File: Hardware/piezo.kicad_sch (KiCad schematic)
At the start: 0 parts

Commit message: Piezo transducer driver added(transistor amplifier part).
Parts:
- added C? (x5): C_Small, symbol Device:C_Small
- added C? (x2): 100n, symbol Device:C_Small
- added C? (x2): 12p %5, Capacitor_SMD:C_0603_1608Metric_Pad1.08x0.95mm_HandSolder, symbol Device:C_Small
- added C?: 100n, Capacitor_SMD:C_0603_1608Metric_Pad1.08x0.95mm_HandSolder, symbol Device:C_Small
- added C?: 220u, symbol LibreSolar:CP
- added C?: 10u, symbol Device:C_Small
- added D? (x2): 1N4148, symbol Device:D_Small
- added J?: AudioJack2, symbol Connector:AudioJack2
- added Q? (x2): BCP53-16, Package_TO_SOT_SMD:SOT-223-3_TabPin2, symbol Transistor_BJT:BCP53
- added Q? (x2): BC817, Package_TO_SOT_SMD:SOT-23, symbol Transistor_BJT:BC817
- added Q?: MJD44H11T4G, symbol Device:Q_PNP_BCE
- added Q?: MJD45H11T4G, symbol Device:Q_NPN_BCE
- added Q? (x2): BCP56-16, Package_TO_SOT_SMD:SOT-223-3_TabPin2, symbol Transistor_BJT:BCP56
- added R? (x9): R_Small, symbol Device:R_Small
- added R?: 8.2k %1, Resistor_SMD:R_0603_1608Metric_Pad0.98x0.95mm_HandSolder, symbol Device:R_Small
- added R? (x4): 33R %1, Resistor_SMD:R_0603_1608Metric_Pad0.98x0.95mm_HandSolder, symbol Device:R_Small
- added R? (x3): 2.2k %1, Resistor_SMD:R_0603_1608Metric_Pad0.98x0.95mm_HandSolder, symbol Device:R_Small
- added R? (x2): 422R %1, Resistor_SMD:R_0603_1608Metric_Pad0.98x0.95mm_HandSolder, symbol Device:R_Small
- added R? (x2): 0.33R, Resistor_SMD:R_2512_6332Metric_Pad1.40x3.35mm_HandSolder, symbol Device:R_Small
- added R?: 1.2k %1, Resistor_SMD:R_0603_1608Metric_Pad0.98x0.95mm_HandSolder, symbol Device:R_Small
- added U? (x2): Opamp_Dual, symbol Device:Opamp_Dual
- added U? (x3): LM7322, symbol Device:Opamp_Dual
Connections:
- new net: C?.1, R?.1, R?.2 (x2)
- new net: C?.2, R?.1, U?.1, U?.2 (-) (x2)
- new net: Q?.1 (B), Q?.3 (C), R?.1 (x2)
- new net: C?.2, Q?.1 (B), Q?.1 (B), Q?.2 (C), Q?.2 (C), Q?.4 (C), Q?.4 (C)
- new net: Q?.3 (E), R?.1 (x3)
- new net: R?.1, U?.1
- new net: R?.1, R?.2, U?.2 (-)
- new net: R?.1, R?.2, U?.5 (+)
- new net: J?.T, R?.1, R?.1, R?.1, R?.2
- new net: C?.1, Q?.1 (B), R?.2, R?.2
- new net: C?.1, Q?.1 (B), R?.1, R?.2
- new net: Q?.2 (E), Q?.2 (E), R?.2
- new net: C?.1, D?.1 (K), Q?.1 (B), Q?.2 (C), Q?.4 (C)
- new net: Q?.3 (E), R?.2 (x3)
- new net: C?.1, R?.2, U?.3 (+) (x2)
- new net: C?.2, C?.2, D?.2 (A), Q?.1 (B), Q?.2 (C), Q?.4 (C)
- new net: C?.1, R?.2
- new net: C?.2, J?.S, R?.1
- new net: D?.1 (K), D?.2 (A)
- new net +24V: C?.1, C?.1, C?.1, C?.1, Q?.2 (C), R?.2, R?.2, R?.2, R?.2, R?.2
- new net +5VA: U?.8 (V+)
- new net GND: C?.2, C?.2, C?.2, C?.2, C?.2, C?.2, Q?.2 (C), R?.1, R?.1, R?.1, R?.1, R?.2, R?.2, U?.4 (V-)
- new net amplifier_in: R?.1

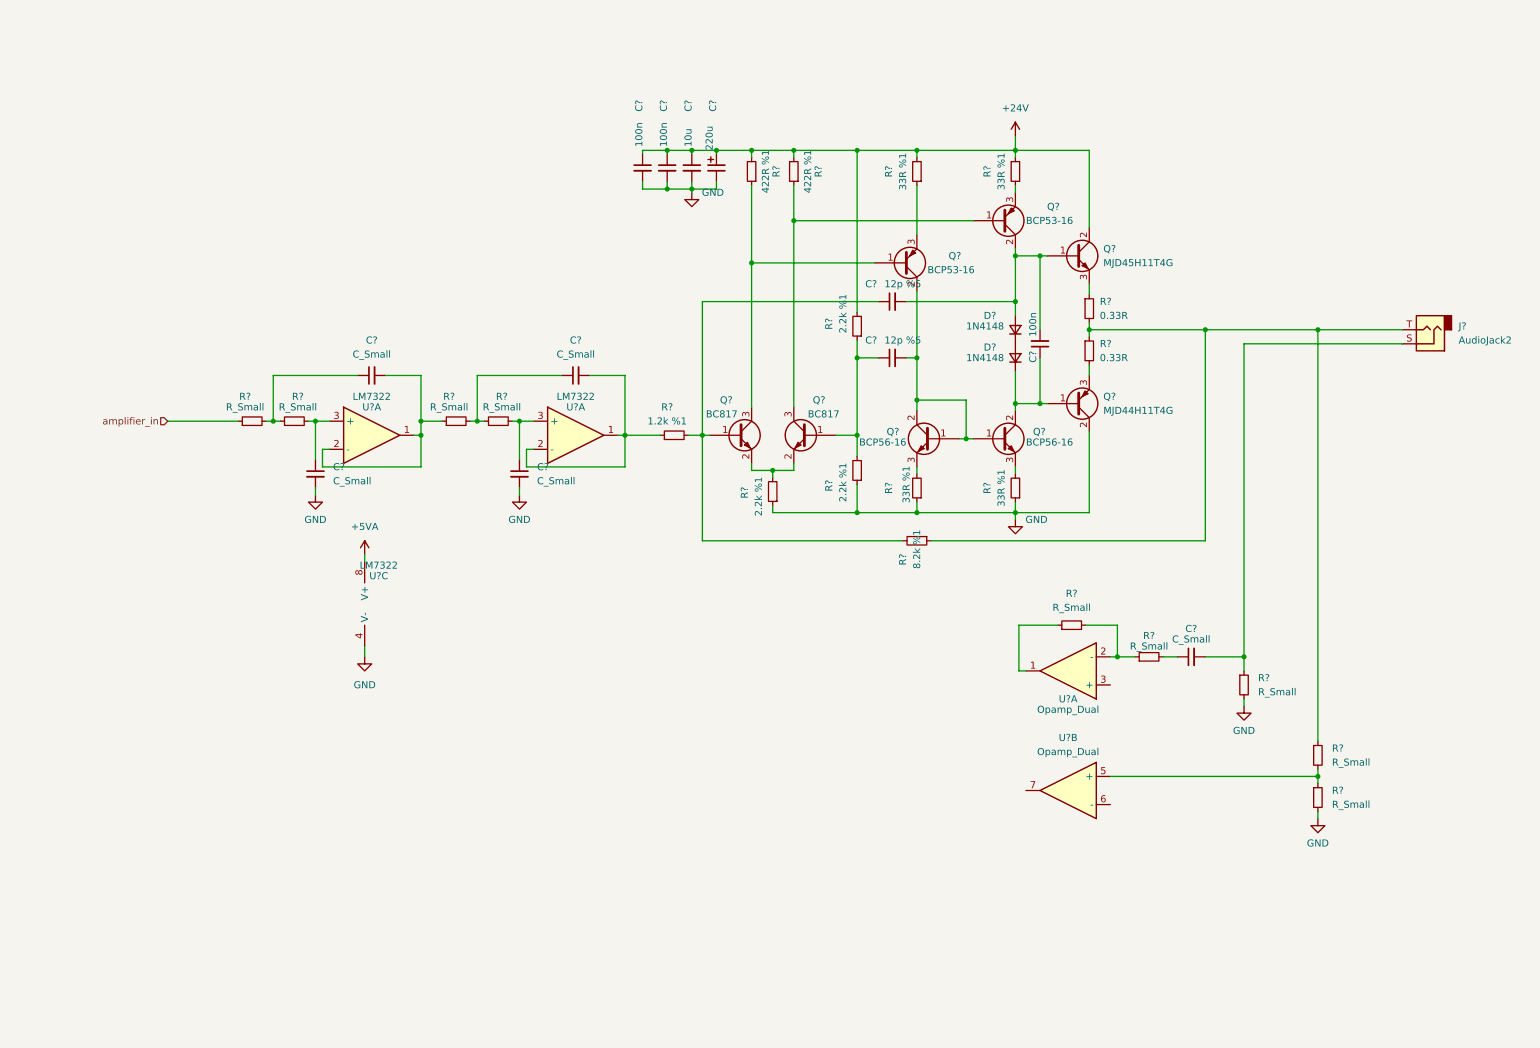
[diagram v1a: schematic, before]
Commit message: Changes about piezo transducer driver
+ Regarding measurement of piezo transducer impedance, driver circuit is updated.(-+15v). Besides circuit is updated. But yet to be simulated for new resistance values.
+ Most cost efficient analog design(up to now) is created. Noise free enough, but nothing more.
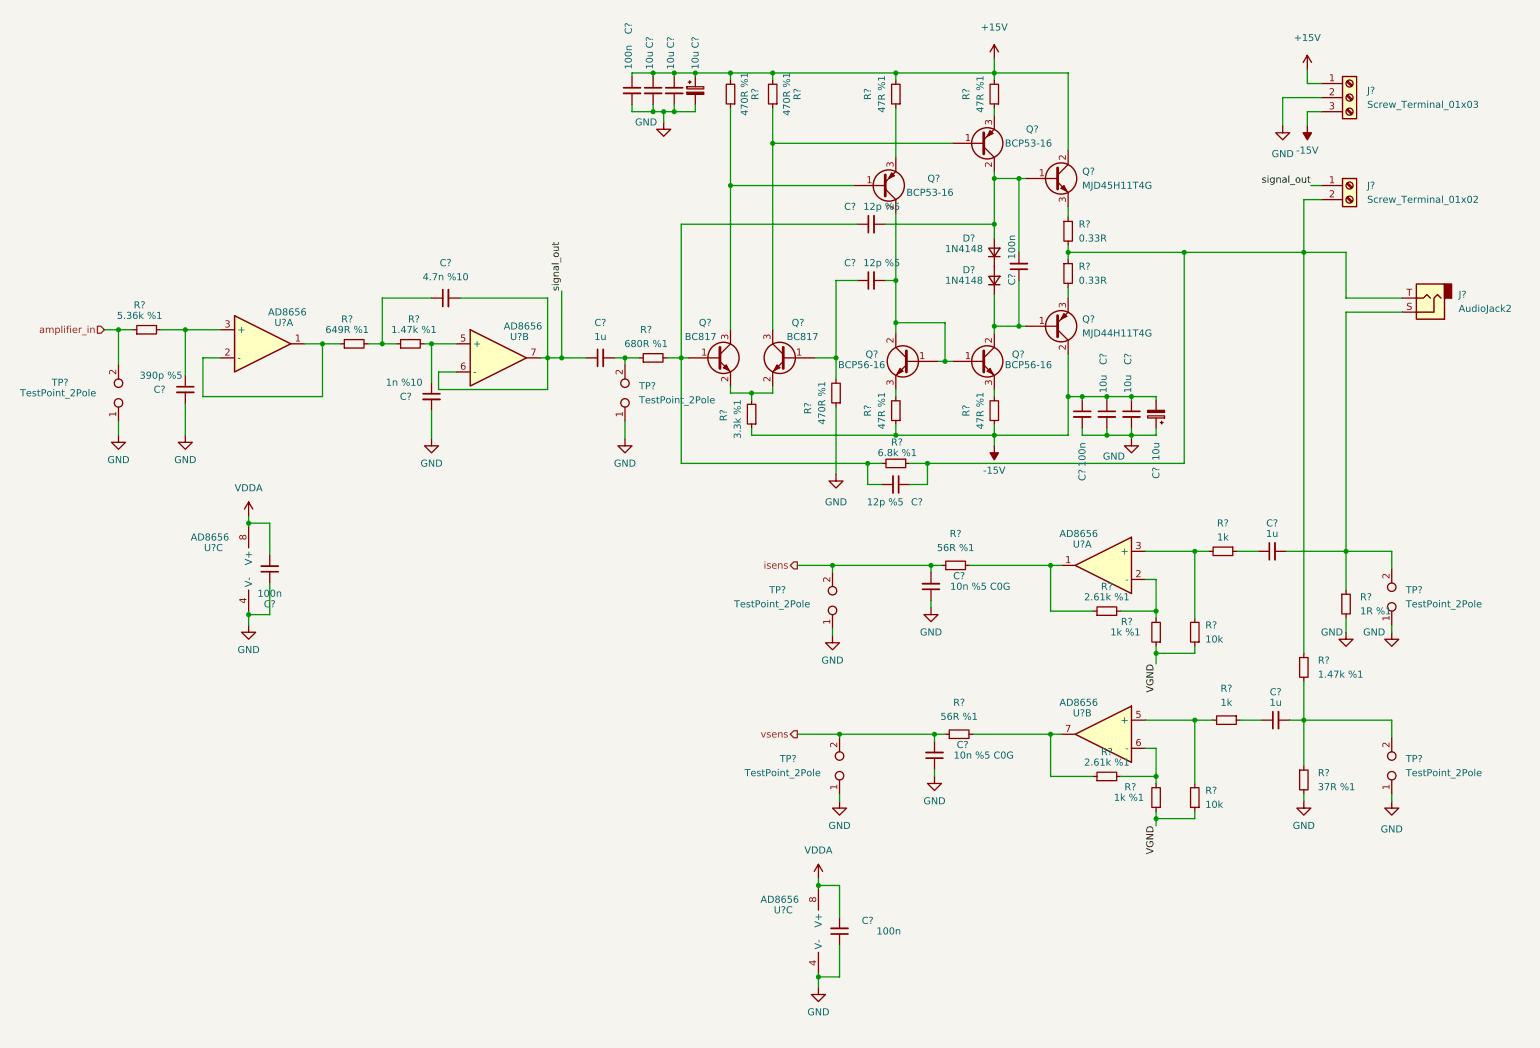
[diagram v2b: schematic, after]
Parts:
- removed C? (x3): C_Small, symbol Device:C_Small
- removed C?: 220u, symbol LibreSolar:CP
- removed C?: 10u, symbol Device:C_Small
- removed C?: 100n, symbol Device:C_Small
- removed R? (x6): R_Small, symbol Device:R_Small
- removed R? (x3): 33R %1, Resistor_SMD:R_0603_1608Metric_Pad0.98x0.95mm_HandSolder, symbol Device:R_Small
- removed R?: 422R %1, Resistor_SMD:R_0603_1608Metric_Pad0.98x0.95mm_HandSolder, symbol Device:R_Small
- removed R?: 2.2k %1, Resistor_SMD:R_0603_1608Metric_Pad0.98x0.95mm_HandSolder, symbol Device:R_Small
- removed U? (x2): Opamp_Dual, symbol Device:Opamp_Dual
- removed U? (x3): LM7322, symbol Device:Opamp_Dual
- added C? (x2): 10n %5 C0G, Capacitor_SMD:C_0603_1608Metric_Pad1.08x0.95mm_HandSolder, symbol Device:C_Small
- added C? (x2): 100n, Capacitor_SMD:C_0603_1608Metric_Pad1.08x0.95mm_HandSolder, symbol Device:C_Small
- added C?: 12p %5, Capacitor_SMD:C_0603_1608Metric_Pad1.08x0.95mm_HandSolder, symbol Device:C_Small
- added C? (x4): 10u, symbol Device:C_Small
- added C? (x2): 1u, symbol Device:C_Small
- added C?: 100n, symbol Device:C_Small
- added C?: 390p %5, symbol Device:C_Small
- added C?: 1n %10, symbol Device:C_Small
- added C? (x2): 10u, symbol Device:C_Polarized_Small
- added J?: Screw_Terminal_01x03, symbol Connector:Screw_Terminal_01x03
- added J?: Screw_Terminal_01x02, symbol Connector:Screw_Terminal_01x02
- added R? (x2): 1k %1, symbol Device:R_Small
- added R? (x3): 47R %1, Resistor_SMD:R_0603_1608Metric_Pad0.98x0.95mm_HandSolder, symbol Device:R_Small
- added R?: 5.36k %1, Resistor_SMD:R_0603_1608Metric_Pad0.98x0.95mm_HandSolder, symbol Device:R_Small
- added R?: 470R %1, Resistor_SMD:R_0603_1608Metric_Pad0.98x0.95mm_HandSolder, symbol Device:R_Small
- added R? (x2): 2.61k %1, symbol Device:R_Small
- added R? (x2): 1k, symbol Device:R_Small
- added R?: 37R %1, symbol Device:R_Small
- added R?: 1.47k %1, symbol Device:R_Small
- added R? (x2): 56R %1, symbol Device:R_Small
- added R? (x2): 10k, symbol Device:R_Small
- added TP? (x6): TestPoint_2Pole, symbol Connector:TestPoint_2Pole
- added U? (x6): AD8656, Package_SO:SOIC-8_3.9x4.9mm_P1.27mm, symbol Device:Opamp_Dual
- C?: value C_Small -> 4.7n %10
- C?: value C_Small -> 1u
- R?: value 8.2k %1 -> 6.8k %1; Link https://ozdisan.com/passive-components/resistors/smt-smd-an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 -> (none); Price 0.00221 -> (none)
- R?: value 2.2k %1 -> 470R %1; Link https://ozdisan.com/passive-components/resistors/smt-smd-an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 -> (none); Price 0.00221 -> (none)
- R?: value R_Small -> 649R %1; footprint (none) -> Resistor_SMD:R_0603_1608Metric_Pad0.98x0.95mm_HandSolder
- R?: value 2.2k %1 -> 3.3k %1; Link https://ozdisan.com/passive-components/resistors/smt-smd-an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 -> (none); Price 0.00221 -> (none)
- R?: value R_Small -> 1R %1
- R?: value R_Small -> 1.47k %1; footprint (none) -> Resistor_SMD:R_0603_1608Metric_Pad0.98x0.95mm_HandSolder
- R?: value 422R %1 -> 470R %1; Link https://ozdisan.com/passive-components/resistors/smt-smd-an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 -> (none); Price 0.00364 -> (none)
- R?: value 1.2k %1 -> 680R %1; Link https://ozdisan.com/passive-components/resistors/smt-smd-an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 -> (none); Price 0.00221 -> (none)
- R?: value 33R %1 -> 47R %1; Link https://ozdisan.com/passive-components/resistors/smt-smd-an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 -> (none); Price 0.00221 -> (none)
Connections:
- net GND: now also C?.1, C?.1, C?.1, C?.1, C?.1, C?.2, C?.2, C?.2, C?.2, C?.2, C?.2, C?.2, C?.2, J?.2 (Pin_2), R?.2, TP?.1, TP?.1, TP?.1, TP?.1, TP?.1, TP?.1, U?.4 (V-), U?.4 (V-); no longer Q?.2 (C), R?.1
- net amplifier_in: now also R?.1, TP?.2; no longer R?.1
- net signal_out: now reaches C?.2
- net signal_out: now also C?.1, J?.1 (Pin_1), U?.6 (-), U?.7
- net at J?.T, R?.1, R?.1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: now also C?.1, J?.2 (Pin_2), R?.1
- net at C?.1, Q?.1 (B), R?.2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: now also C?.2
- net at Q?.1 (B), Q?.3 (C): now also R?.1
- net at Q?.3 (E): now also R?.1
- net at R?.2: now also C?.1, U?.5 (+)
- net at C?.1: now also R?.1
- net at Q?.3 (E): now also R?.2 (x2)
- net at R?.1: now also C?.2, TP?.2
- net at C?.2, J?.S, R?.1: now also TP?.2
- net +24V renamed +15V
- net +15V: now also C?.1, C?.1, C?.1, J?.1 (Pin_1), R?.2, R?.2
- new net: R?.1, U?.1, U?.2 (-)
- new net: C?.1, R?.2, U?.3 (+)
- new net: R?.2, R?.2, U?.5 (+)
- new net: R?.2, R?.2, U?.6 (-)
- new net: R?.1, R?.2, U?.7
- new net: R?.2, R?.2, U?.2 (-)
- new net: R?.1, R?.2, U?.1
- new net: R?.2, R?.2, U?.3 (+)
- new net: C?.2, R?.1, R?.2, TP?.2
- new net: C?.1, R?.1
- new net -15V: C?.1, C?.1, C?.1, C?.2, J?.3 (Pin_3), Q?.2 (C), R?.1, R?.1, R?.1
- new net VDDA: C?.2, C?.2, U?.8 (V+), U?.8 (V+)
- new net VGND: R?.1, R?.1, R?.1, R?.1
- new net isens: C?.2, R?.1, TP?.2
- new net vsens: C?.2, R?.1, TP?.2
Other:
- moved on the sheet: C?, D?, J?, Q?, R?

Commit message: Completed schematic and PCB.
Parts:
- removed C?: 4.7n %10, symbol Device:C_Small
- removed C? (x2): 12p %5, Capacitor_SMD:C_0603_1608Metric_Pad1.08x0.95mm_HandSolder, symbol Device:C_Small
- removed C?: 10n %5 C0G, Capacitor_SMD:C_0603_1608Metric_Pad1.08x0.95mm_HandSolder, symbol Device:C_Small
- removed C? (x4): 10u, symbol Device:C_Small
- removed C? (x3): 1u, symbol Device:C_Small
- removed C?: 390p %5, symbol Device:C_Small
- removed C?: 1n %10, symbol Device:C_Small
- removed C? (x2): 10u, symbol Device:C_Polarized_Small
- removed D?: 1N4148, symbol Device:D_Small
- removed J?: Screw_Terminal_01x03, symbol Connector:Screw_Terminal_01x03
- removed J?: Screw_Terminal_01x02, symbol Connector:Screw_Terminal_01x02
- removed Q? (x2): BCP53-16, Package_TO_SOT_SMD:SOT-223-3_TabPin2, symbol Transistor_BJT:BCP53
- removed Q? (x2): BC817, Package_TO_SOT_SMD:SOT-23, symbol Transistor_BJT:BC817
- removed R? (x2): 1k %1, symbol Device:R_Small
- removed R?: 5.36k %1, Resistor_SMD:R_0603_1608Metric_Pad0.98x0.95mm_HandSolder, symbol Device:R_Small
- removed R? (x2): 470R %1, Resistor_SMD:R_0603_1608Metric_Pad0.98x0.95mm_HandSolder, symbol Device:R_Small
- removed R? (x2): 2.61k %1, symbol Device:R_Small
- removed R? (x3): 47R %1, Resistor_SMD:R_0603_1608Metric_Pad0.98x0.95mm_HandSolder, symbol Device:R_Small
- removed R? (x2): 1k, symbol Device:R_Small
- removed R? (x2): 10k, symbol Device:R_Small
- removed R?: 1.47k %1, Resistor_SMD:R_0603_1608Metric_Pad0.98x0.95mm_HandSolder, symbol Device:R_Small
- removed R?: 680R %1, Resistor_SMD:R_0603_1608Metric_Pad0.98x0.95mm_HandSolder, symbol Device:R_Small
- removed R?: 56R %1, symbol Device:R_Small
- removed TP? (x5): TestPoint_2Pole, symbol Connector:TestPoint_2Pole
- removed U?: AD8656, Package_SO:SOIC-8_3.9x4.9mm_P1.27mm, symbol Device:Opamp_Dual
- added C? (x2): 6.8n %5, Capacitor_SMD:C_0805_2012Metric_Pad1.18x1.45mm_HandSolder, symbol Device:C_Small
- added C? (x3): 1u 25v, Capacitor_SMD:C_0603_1608Metric_Pad1.08x0.95mm_HandSolder, symbol Device:C_Small
- added C? (x4): 12p %5, Capacitor_SMD:C_0603_1608Metric_Pad1.08x0.95mm_HandSolder, symbol Device:C_Small
- added C? (x2): 10u 25V, Capacitor_SMD:C_1206_3216Metric_Pad1.33x1.80mm_HandSolder, symbol Device:C_Small
- added C?: 10n %5 C0G, Capacitor_SMD:C_0603_1608Metric_Pad1.08x0.95mm_HandSolder, symbol Device:C_Small
- added C?: 680p %5, Capacitor_SMD:C_0603_1608Metric_Pad1.08x0.95mm_HandSolder, symbol Device:C_Small
- added D?: 1N4148, Diode_SMD:D_SOD-123, symbol Device:D_Small
- added Q? (x2): BC817-40, Package_TO_SOT_SMD:SOT-23, symbol Transistor_BJT:BC817
- added Q? (x2): BCP53-16, Package_TO_SOT_SMD:SOT-223-3_TabPin2, symbol Transistor_BJT:BCP53
- added R? (x2): 536R %1, Resistor_SMD:R_0603_1608Metric_Pad0.98x0.95mm_HandSolder, symbol Device:R_Small
- added R?: 470R %1, Resistor_SMD:R_0603_1608Metric_Pad0.98x0.95mm_HandSolder, symbol Device:R_Small
- added R? (x4): 0R, symbol Device:R_Small
- added R? (x2): 1M, symbol Device:R_Small
- added R? (x2): 680R %1, Resistor_SMD:R_0603_1608Metric_Pad0.98x0.95mm_HandSolder, symbol Device:R_Small
- added R? (x2): 8.2k %1, Resistor_SMD:R_0603_1608Metric_Pad0.98x0.95mm_HandSolder, symbol Device:R_Small
- added R? (x3): 47R %1, Resistor_SMD:R_0603_1608Metric_Pad0.98x0.95mm_HandSolder, symbol Device:R_Small
- added R?: 2.2k %1, Resistor_SMD:R_0603_1608Metric_Pad0.98x0.95mm_HandSolder, symbol Device:R_Small
- added R?: 1430R %1, Resistor_SMD:R_0603_1608Metric_Pad0.98x0.95mm_HandSolder, symbol Device:R_Small
- added R?: 2.15k %1, Resistor_SMD:R_0603_1608Metric_Pad0.98x0.95mm_HandSolder, symbol Device:R_Small
- added R?: 56R %1, Resistor_SMD:R_0603_1608Metric_Pad0.98x0.95mm_HandSolder, symbol Device:R_Small
- added TP? (x6): TestPoint_2Pole, Connector_PinHeader_2.54mm:PinHeader_1x02_P2.54mm_Vertical, symbol Connector:TestPoint_2Pole
- added U?: AD8656, Package_SO:SOIC-8_3.9x4.9mm_P1.27mm, symbol Device:Opamp_Dual
- C? (x2): footprint (none) -> Capacitor_SMD:C_0603_1608Metric_Pad1.08x0.95mm_HandSolder; Link (none) -> https://ozdisan.com/passive-components/capacitors/smt-smd-a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
- C? (x2): Link (none) -> https://ozdisan.com/passive-components/capacitors/smt-smd-a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; Price (none) -> 0.00448
- D?: footprint (none) -> Diode_SMD:D_SOD-123; Link (none) -> https://ozdisan.com/power-semiconductors/diodes-diode-modul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; Price (none) -> 0.02794
- Q?: footprint (none) -> Package_TO_SOT_SMD:TO-252-2; Link (none) -> https://ozdisan.com/Product/Detail/448869/MJD44H11T4G; Price (none) -> 0.39273
- Q?: footprint (none) -> Package_TO_SOT_SMD:TO-252-2; Link (none) -> https://ozdisan.com/Product/Detail/448870/MJD45H11T4G; Price (none) -> 0.55649
- R?: value 6.8k %1 -> 8.2k %1; Link (none) -> https://ozdisan.com/passive-components/resistors/smt-smd-an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; Price (none) -> 0.00221
- R? (x3): Link (none) -> https://ozdisan.com/passive-components/resistors/smt-smd-an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; Price (none) -> 0.00221
- R?: value 649R %1 -> 887R %1; Link (none) -> https://ozdisan.com/passive-components/resistors/smt-smd-an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; Price (none) -> 0.00221
- R?: value 37R %1 -> 61.9R %1; footprint (none) -> Resistor_SMD:R_0603_1608Metric_Pad0.98x0.95mm_HandSolder; Link (none) -> https://ozdisan.com/passive-components/resistors/smt-smd-an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; Price (none) -> 0.00221
- R?: value 1.47k %1 -> 2.2k %1; footprint (none) -> Resistor_SMD:R_0603_1608Metric_Pad0.98x0.95mm_HandSolder; Link (none) -> https://ozdisan.com/passive-components/resistors/smt-smd-an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; Price (none) -> 0.00221
- R?: footprint (none) -> Resistor_SMD:R_0603_1608Metric_Pad0.98x0.95mm_HandSolder; Link (none) -> https://ozdisan.com/passive-components/resistors/smt-smd-an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; Price (none) -> 0.00221
- R?: value 1R %1 -> 1R 1/3W %1; footprint (none) -> Resistor_SMD:R_1210_3225Metric_Pad1.30x2.65mm_HandSolder; Link (none) -> https://ozdisan.com/passive-components/resistors/smt-smd-an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; Price (none) -> 0.05112
- TP?: footprint (none) -> Connector_PinHeader_2.54mm:PinHeader_1x02_P2.54mm_Vertical; Link (none) -> https://ozdisan.com/connectors-and-interconnects/headers/pi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; Price (none) -> 0.0091
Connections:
- net amplifier_in is gone; now on net SIGNAL: TP?.2
- net +15V: now also C?.1, R?.2, R?.2, R?.2
- net -15V: now also C?.1, R?.1
- net GND: now also C?.1, C?.2, C?.2, C?.2, C?.2, R?.1, TP?.1, TP?.1, TP?.1, TP?.1, TP?.1
- net at R?.2: now also C?.1, R?.1, R?.1
- net at R?.1: now also Q?.1 (B), Q?.3 (C)
- net at Q?.1 (B), Q?.1 (B), Q?.2 (C)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: now also C?.2, Q?.2 (C), Q?.4 (C), R?.1
- net at J?.S, R?.1: now also C?.2, TP?.2
- net at U?.1, U?.2 (-): now also R?.1; no longer R?.1
- net SIGNAL: now reaches U?.3 (+)
- net at J?.T, R?.1, R?.1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: now also C?.1, TP?.1
- net at R?.2: now also C?.2, R?.1; no longer C?.1
- net at R?.2: now also Q?.2 (E), Q?.2 (E)
- net at C?.1, Q?.1 (B), Q?.2 (C)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: now also D?.1 (K), R?.2
- net at R?.2: now also C?.1, R?.1, U?.7
- net at U?.2 (-): now also C?.2, R?.1, R?.1
- net at C?.2, C?.2, D?.2 (A)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: now also Q?.2 (C), Q?.4 (C), R?.2
- net at Q?.3 (E), R?.1: now also TP?.2
- net at U?.1: now also C?.1, R?.2, R?.2
- net v1.65: now reaches U?.3 (+)
- net v1.65: now also U?.5 (+), U?.5 (+)
- net at Q?.3 (E): now also R?.2
- net at R?.1, R?.2: now also C?.2, TP?.2
- net at D?.1 (K): now also D?.2 (A), R?.1
- net isens renamed ISENS
- net ISENS: now also R?.1, TP?.2
- net signal_out: no longer names the net of U?.6 (-)
- net signal_out: now also C?.1, R?.2; no longer U?.7
- net vsens renamed VSENS
- net VSENS: now also C?.2, TP?.2
- new net: Q?.1 (B), R?.1, R?.2, R?.2
- new net: Q?.1 (B), Q?.3 (C), R?.1
- new net: Q?.3 (E), R?.1 (x2)
- new net: C?.1, R?.2, R?.2
- new net: C?.1, R?.2 (x2)
- new net: C?.2, R?.2
- new net: C?.1, R?.1, R?.2
- new net: Q?.1 (B), R?.1, R?.2
- new net: C?.2, R?.1, R?.2, U?.6 (-)
- new net: C?.1, R?.1, R?.1
- new net: C?.1, C?.2, R?.2, TP?.2, U?.7
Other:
- moved on the sheet: C?, D?, Q?, R?, TP?, U?A, U?B, U?C
